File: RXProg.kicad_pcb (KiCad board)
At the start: 6 copper layers, 18.8 x 36.6 mm, 25 parts, among them J1 Conn_01x14, J2 Conn_01x14, J3 Pin, J4 Pin, J5 USB_B_Micro, J6 SWD, U1 STM32G474CETx, U2 SN74ALVC164245DGG, U3 TXU0104RUTR, U4 MIC5317-3.3xM5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

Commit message: Fix vias
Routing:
- net D5: track 17.2 -> 14.3 mm
- net A10: track 14.6 -> 16.2 mm
- net Net-(U1-PB5): track 0.47 -> 2.10 mm
- net Net-(U1-PB10): track 16.0 -> 17.4 mm
- net Net-(U1-PB15): track 13.5 -> 14.2 mm
- net ~{CS1}: track 20.2 -> 20.8 mm
- net Net-(U1-PA0): track 14.4 -> 15.0 mm

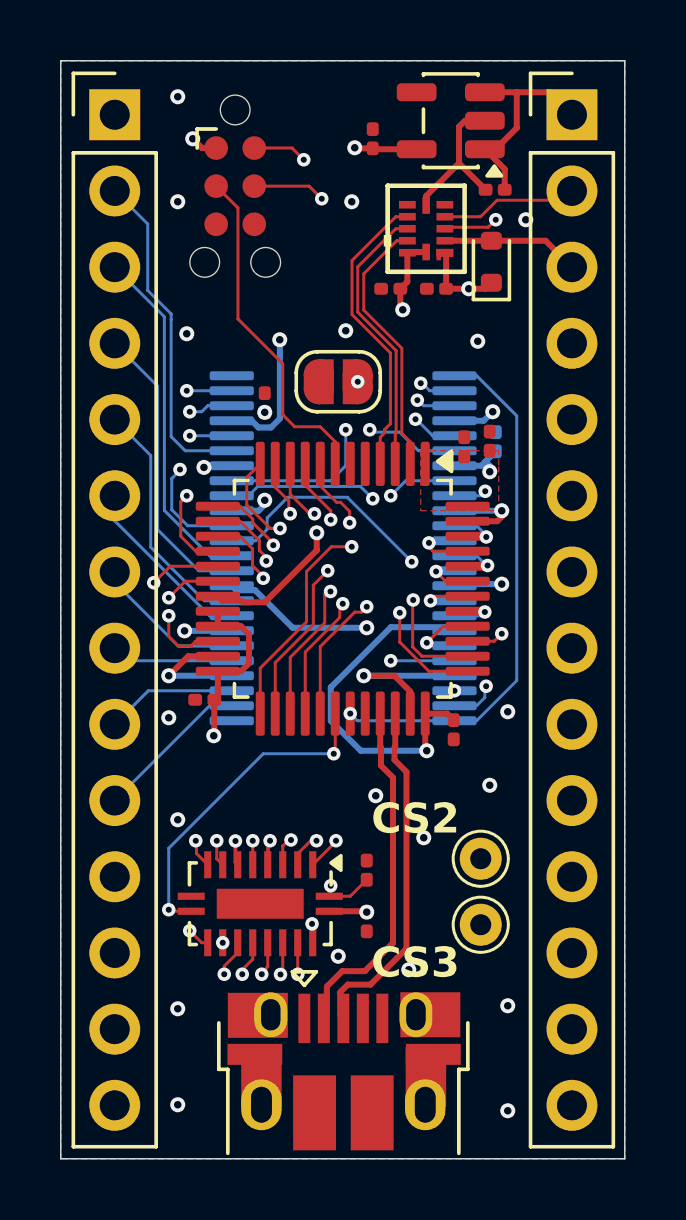
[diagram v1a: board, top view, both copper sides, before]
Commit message: Add jumper text
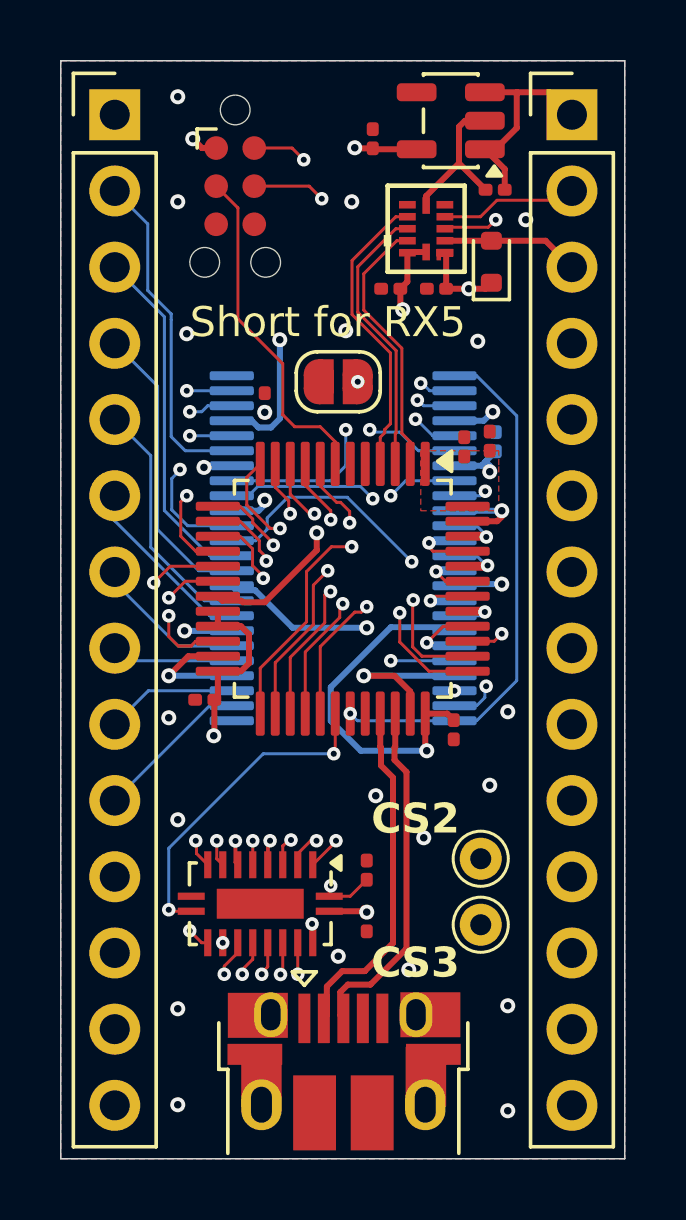
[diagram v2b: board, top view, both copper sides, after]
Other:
- board text added: "Short for RX5"
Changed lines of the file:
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@@
 		(layer "Edge.Cuts")
+	)
+	(gr_text "Short for RX5"
+		(at 121.1 99.1 0)
+		(layer "F.SilkS")
+		(effects
+			(font
+				(size 1 1)
+				(thickness 0.15)
+			)
+			(justify left bottom)
+		)
 	)
 	(gr_text "CS2"
